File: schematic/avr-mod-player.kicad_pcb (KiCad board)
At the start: 2 copper layers, 100 x 60 mm, 49 parts, among them J1 USBasp header, J2 DC-005 Power Jack, J3 RCA AV2-8.4-45, J4 Conn_02x04_Odd_Even, U1 ATmega32A-P, U2 AM29F040B-90PC, U3 74HC595, U4 MCP6022, U5 L7805, Y1 16 MHz

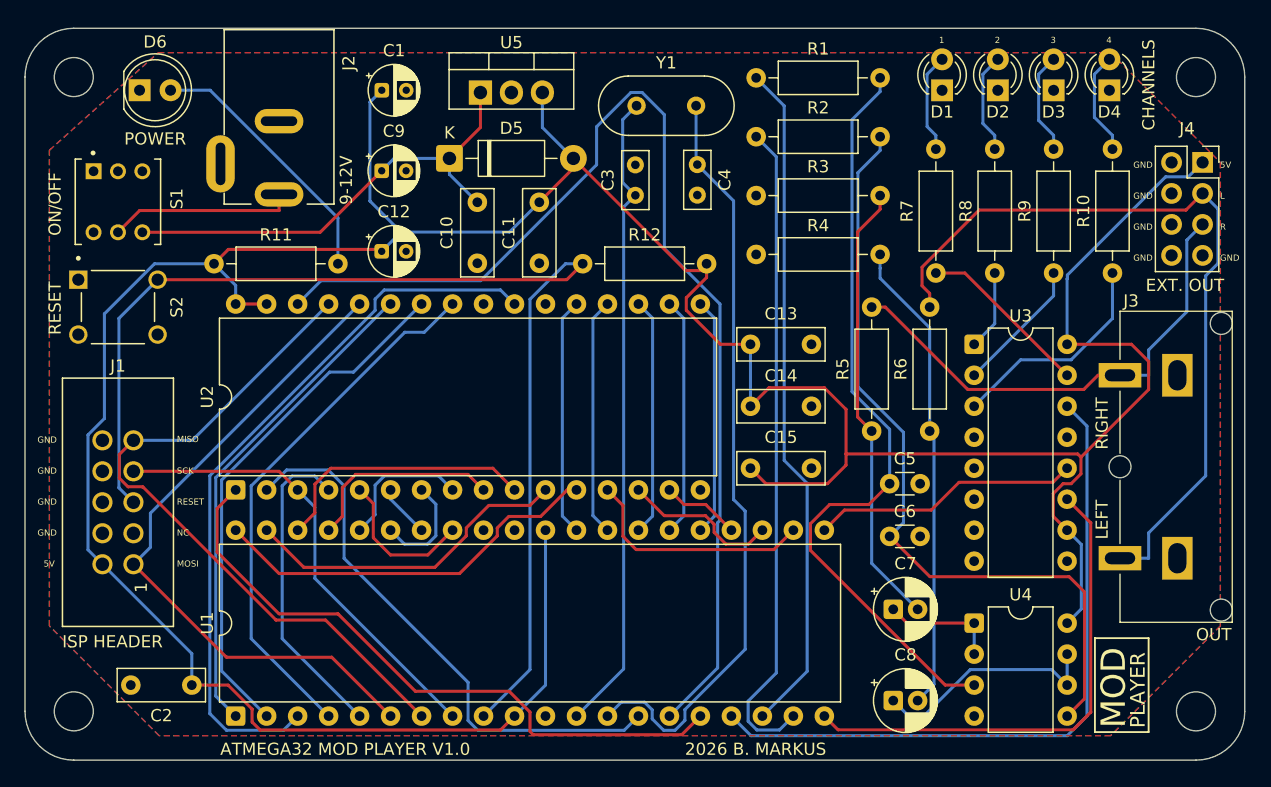
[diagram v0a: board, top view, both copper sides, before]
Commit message: Schottky diode added to ISP header for protection
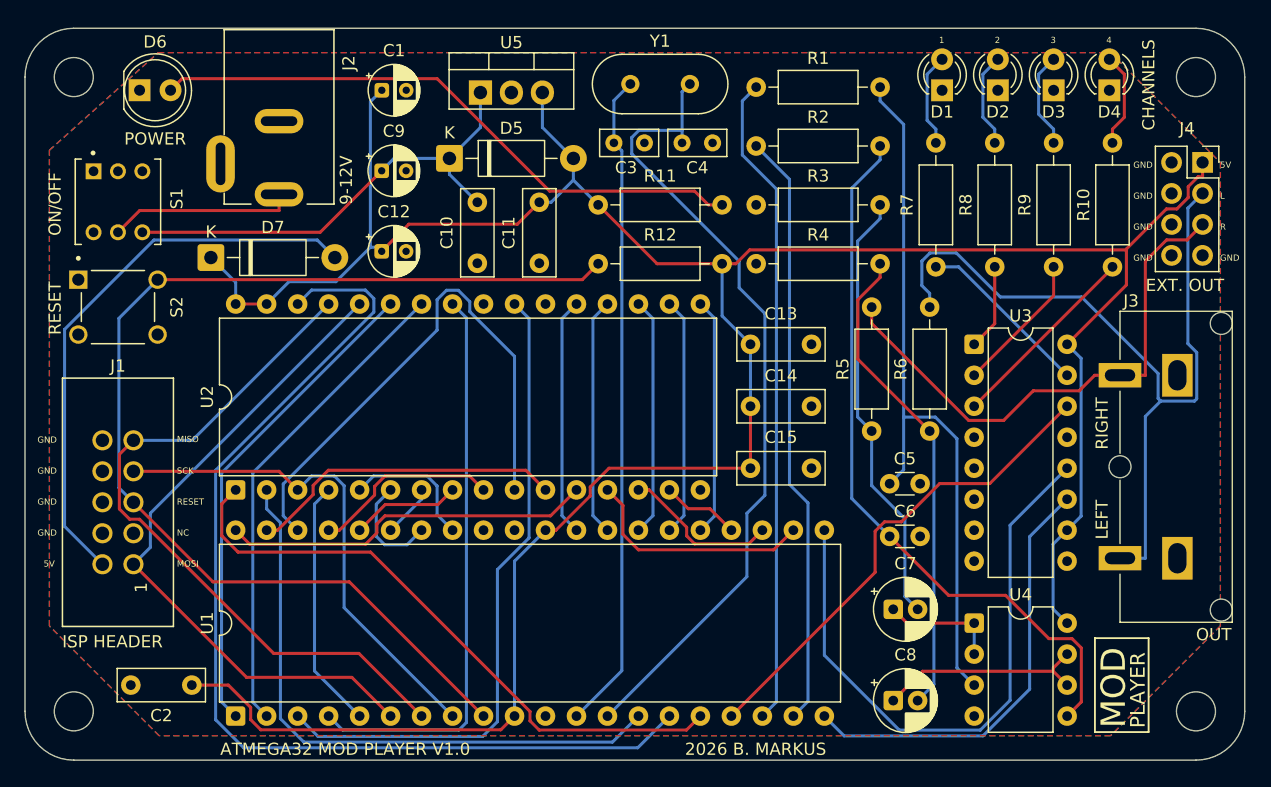
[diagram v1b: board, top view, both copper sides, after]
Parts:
- added D7: 1N5819, Diode_THT:D_DO-41_SOD81_P10.16mm_Horizontal, F.Cu at (15.2, 18.8)
- moved R11 31.9 mm to (47.0, 14.5)
- moved C3 4.64 mm to (48.3, 9.40), turned to 0 degrees
- moved C4 2.17 mm to (53.9, 9.40), turned to 0 degrees
- moved Y1 1.85 mm to (49.6, 4.57)
- moved R12 1.27 mm to (47.0, 19.3)
- moved R3 0.76 mm to (59.9, 14.5)
- moved R1 0.76 mm to (59.9, 4.83)
- moved R2 0.76 mm to (59.9, 9.65)
- moved R4 0.76 mm to (59.9, 19.3)
- moved R10 0.51 mm to (89.2, 19.6)
- moved R7 0.51 mm to (74.7, 19.6)
- moved R8 0.51 mm to (79.5, 19.6)
- moved R9 0.51 mm to (84.3, 19.6)
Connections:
- J1 pad 2: +5V -> Net-(D7-A)
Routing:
- net Net-(D7-A): track 0.00 -> 46.3 mm
- net +5V: track 277.6 -> 234.3 mm
- net Net-(D6-A): track 21.8 -> 49.9 mm
- net Net-(U1-PD7): track 22.0 -> 50.0 mm
- net /A2: track 22.0 -> 44.9 mm
- net Net-(U1-PD3): track 56.6 -> 40.0 mm
- net /A10: track 60.1 -> 53.4 mm
- net /A17: track 92.7 -> 86.1 mm
- net /A12: track 26.1 -> 20.6 mm
- net Net-(U1-PD6): track 41.2 -> 35.9 mm
- net Net-(U1-PD5): track 54.0 -> 49.0 mm
- net /A16: track 45.8 -> 50.3 mm
- net /A6: track 4.35 -> 8.78 mm
- net /A5: track 8.71 -> 4.35 mm
- net Net-(U4B-+): track 64.2 -> 59.8 mm
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
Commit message: Schematic: Silkscreen updated on boards
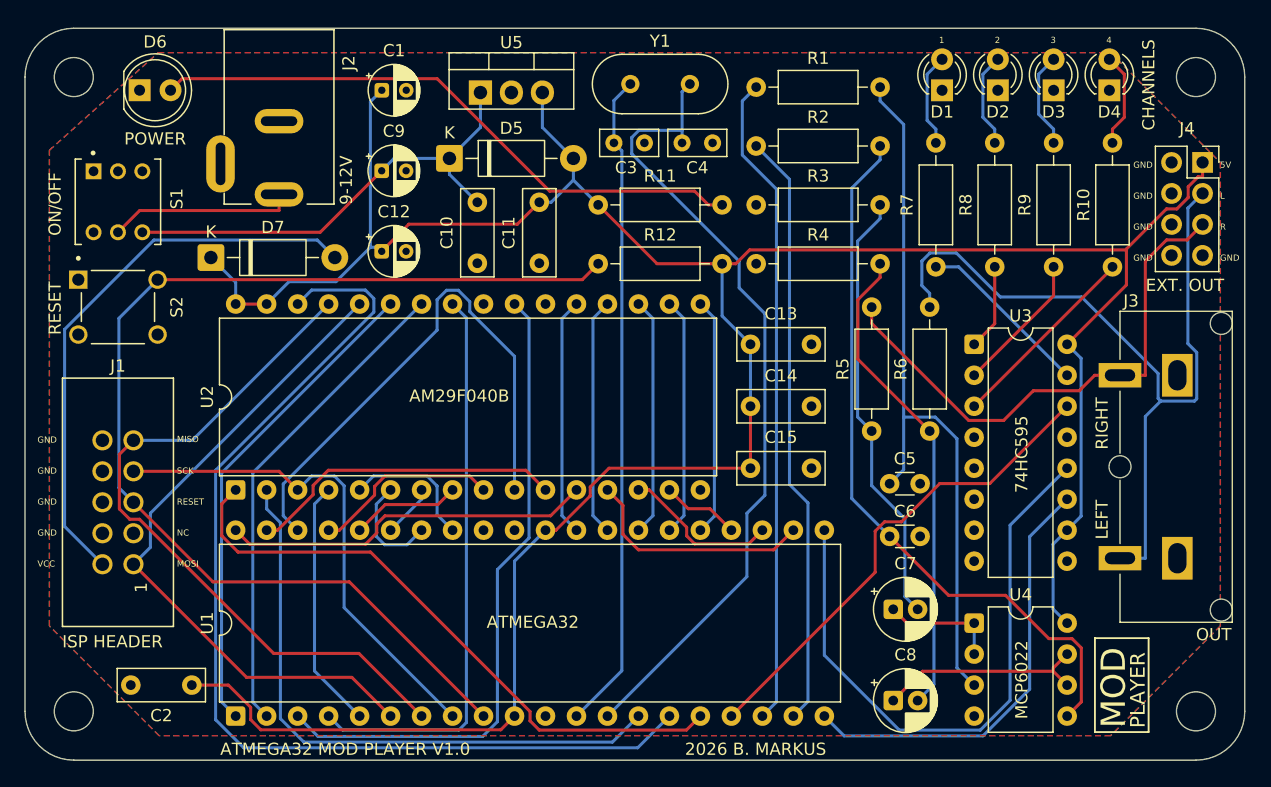
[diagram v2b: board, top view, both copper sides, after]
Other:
- board text added: "74HC595"
- board text added: "AM29F040B"
- board text added: "ATMEGA32"
- board text added: "MCP6022"
- board text added: "VCC"
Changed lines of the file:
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@@
+		)
+	)
+	(gr_text "AM29F040B"
+		(at 31.496 30.734 0)
+		(layer "F.SilkS")
+		(effects
+			(font
+				(size 1 1)
+				(thickness 0.15)
+			)
+			(justify left bottom)
 		)
 	)
@@
 		)
 	)
+	(gr_text "MCP6022"
+		(at 82.296 56.642 90)
+		(layer "F.SilkS")
+		(effects
+			(font
+				(size 1 1)
+				(thickness 0.15)
+			)
+			(justify left bottom)
+		)
+	)
 	(gr_text "RIGHT"
 		(at 88.884 34.544 90)
@@
 		)
 	)
-	(gr_text "5V"
-		(at 1.524 44.196 0)
+	(gr_text "VCC"
+		(at 1.016 44.196 0)
 		(layer "F.SilkS")
 		(effects
@@
 				(size 0.508 0.508)
 				(thickness 0.127)
+			)
+			(justify left bottom)
+		)
+	)
+	(gr_text "74HC595"
+		(at 82.296 38.1 90)
+		(layer "F.SilkS")
+		(effects
+			(font
+				(size 1 1)
+				(thickness 0.15)
 			)
 			(justify left bottom)
@@
 		(layer "F.SilkS")
 		(effects
+			(font
+				(size 1 1)
+				(thickness 0.15)
+			)
+			(justify left bottom)
+		)
+	)
+	(gr_text "ATMEGA32"
+		(at 37.846 49.276 0)
+		(layer "F.SilkS")
+		(effects
